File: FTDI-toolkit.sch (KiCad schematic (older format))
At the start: 86 parts, among them IC1 TLV70033DCKT, IC12 SN74LV1T125DCKR, IC13 74HC00BQ, IC15 TS5A3359, IC2 TLV70018DCKT, IC3 TS5A3359, IC7 SN74LV1T125DCKR, U1 FT2232HQ, Y1 MQ-6.000-12-30/30/

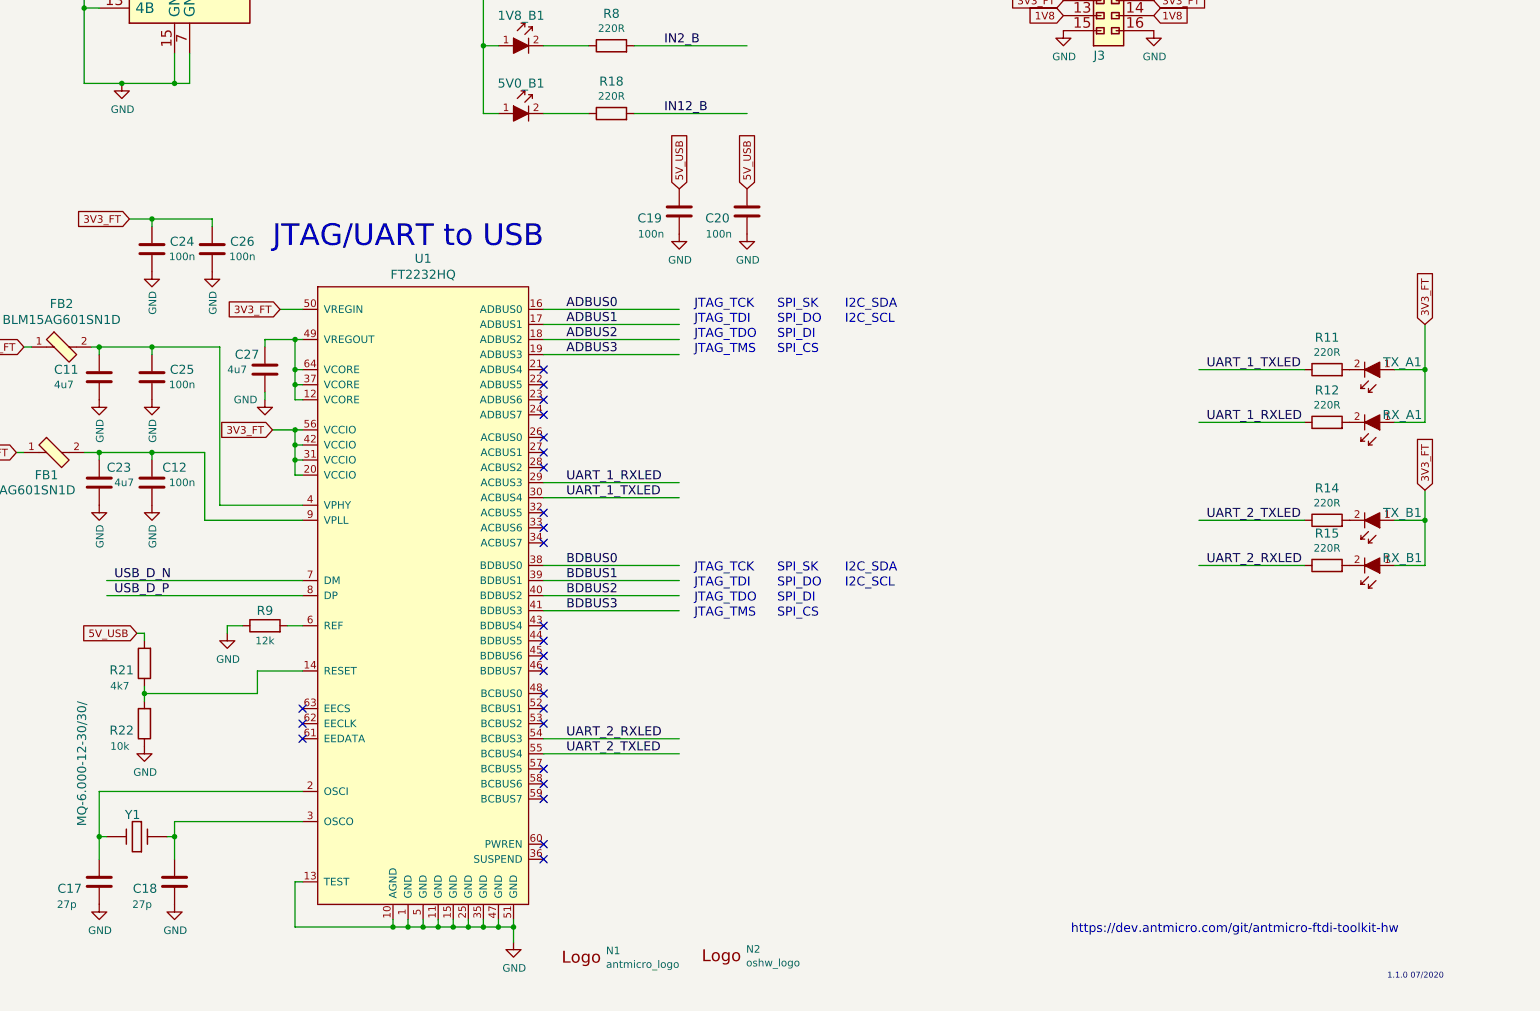
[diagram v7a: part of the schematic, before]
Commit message: Add FT2232H-56Q in a smaller package
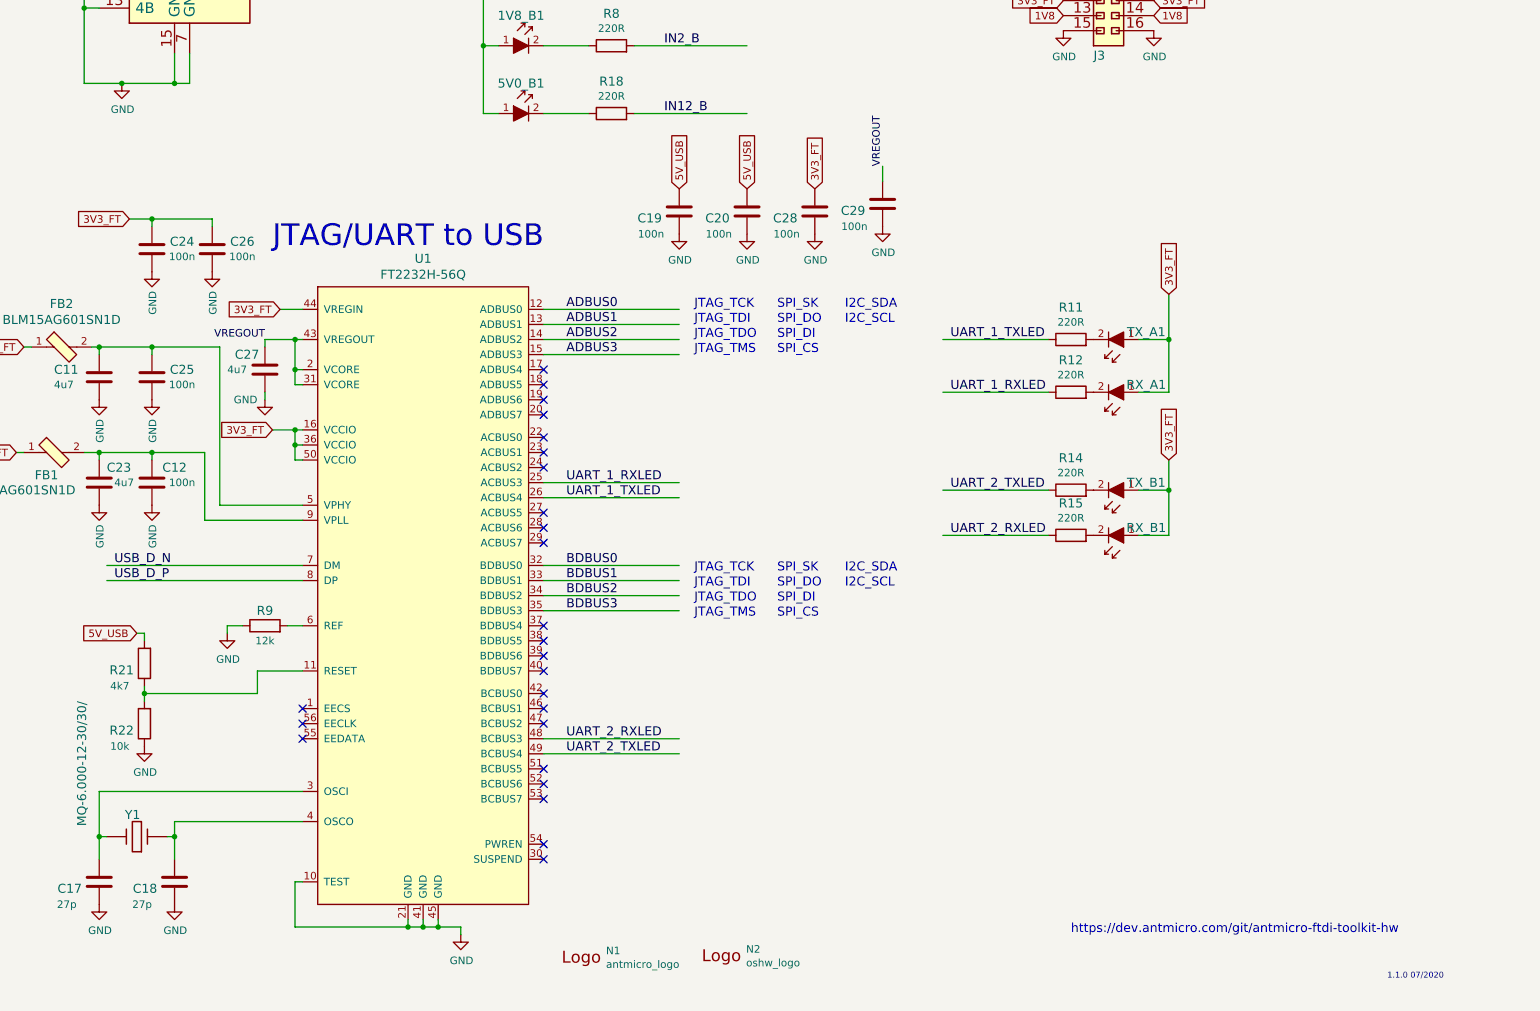
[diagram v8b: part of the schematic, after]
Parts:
- removed U1: FT2232HQ, antmicro-footprints:LQFP-64_10x10mm, symbol antmicroInterfaceControllers:FT2232HQ
- added C28, C29: C_100n_0402_16V, antmicro-footprints:0402-cap, symbol antmicroCapacitors0402:C_100n_0402_16V
- added U1: FT2232H-56Q, antmicro-footprints:QFN-56-1EP_8x8mm_P0.5mm_EP5.5.9x5.9mm, symbol antmicroInterfaceControllers:FT2232H-56Q
- IC10, IC11, IC4, IC6: value ~ -> SN74LV1T125DCKR; footprint FTDI-toolkit:SC70-5 -> antmicro-footprints:SC70-5
- IC5, IC9: value ~ -> SN74LV1T125DCKR
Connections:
- net labels added: VREGOUT
- wire segments 323 -> 309
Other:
- moved on the sheet: R11, R12, R14, R15, RX_A1, RX_B1, TX_A1, TX_B1
